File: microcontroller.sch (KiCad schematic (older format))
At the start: 40 parts, among them P1 SWD, P2 DEBUG_UART, P4 CONN_01X08, P5 CONN_01X08, SW1 SW_PUSH, SW2 SW_PUSH, SW3 SW_PUSH, U2 SN74LVC1G08, U3 STM32F072RB, U4 HDC1080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

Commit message: ready?
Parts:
- removed P4, P5: CONN_01X08, Pin_Headers:Pin_Header_Straight_1x08, symbol CONN_01X08
- added P4, P5: CONN_02X05, CAN_Node:PIN_Header_SMD_2.54mm_02x05, symbol CONN_02X05
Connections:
- wire segments 170 -> 176

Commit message: Use micro match for debug connector.
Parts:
- removed P1: SWD, Pin_Headers:Pin_Header_Straight_1x05, symbol CONN_01X05
- removed P2: DEBUG_UART, Pin_Headers:Pin_Header_Straight_1x03, symbol CONN_01X03
- added P1: Debug, CAN_Node:micromatch_smd_2x05, symbol CONN_02X05
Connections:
- wire segments 176 -> 184

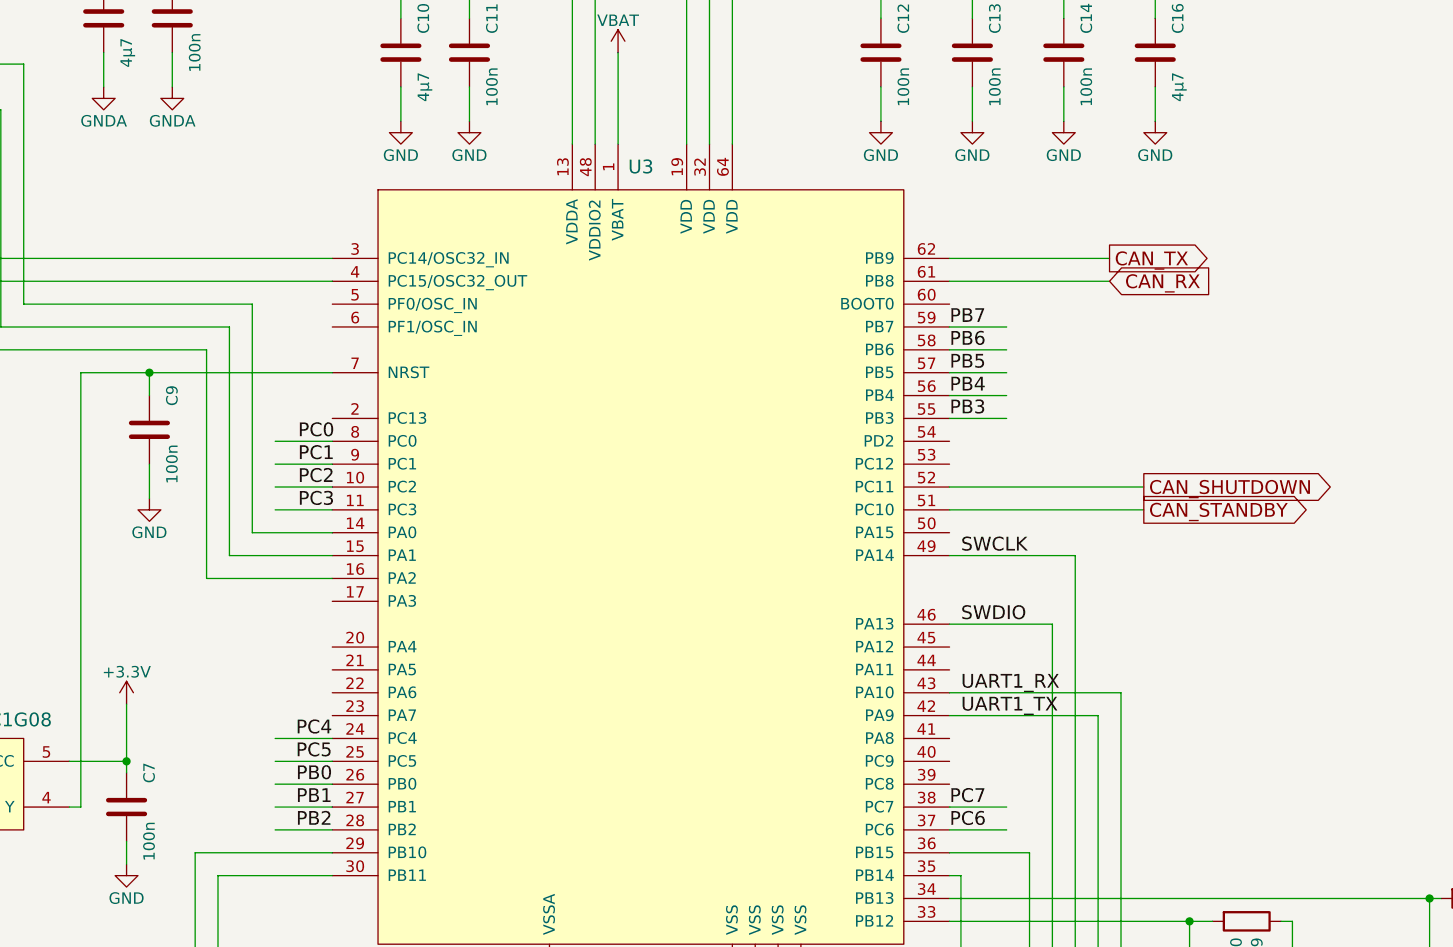
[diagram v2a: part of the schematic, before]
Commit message: Add measurement points, copyright label, minor changes.
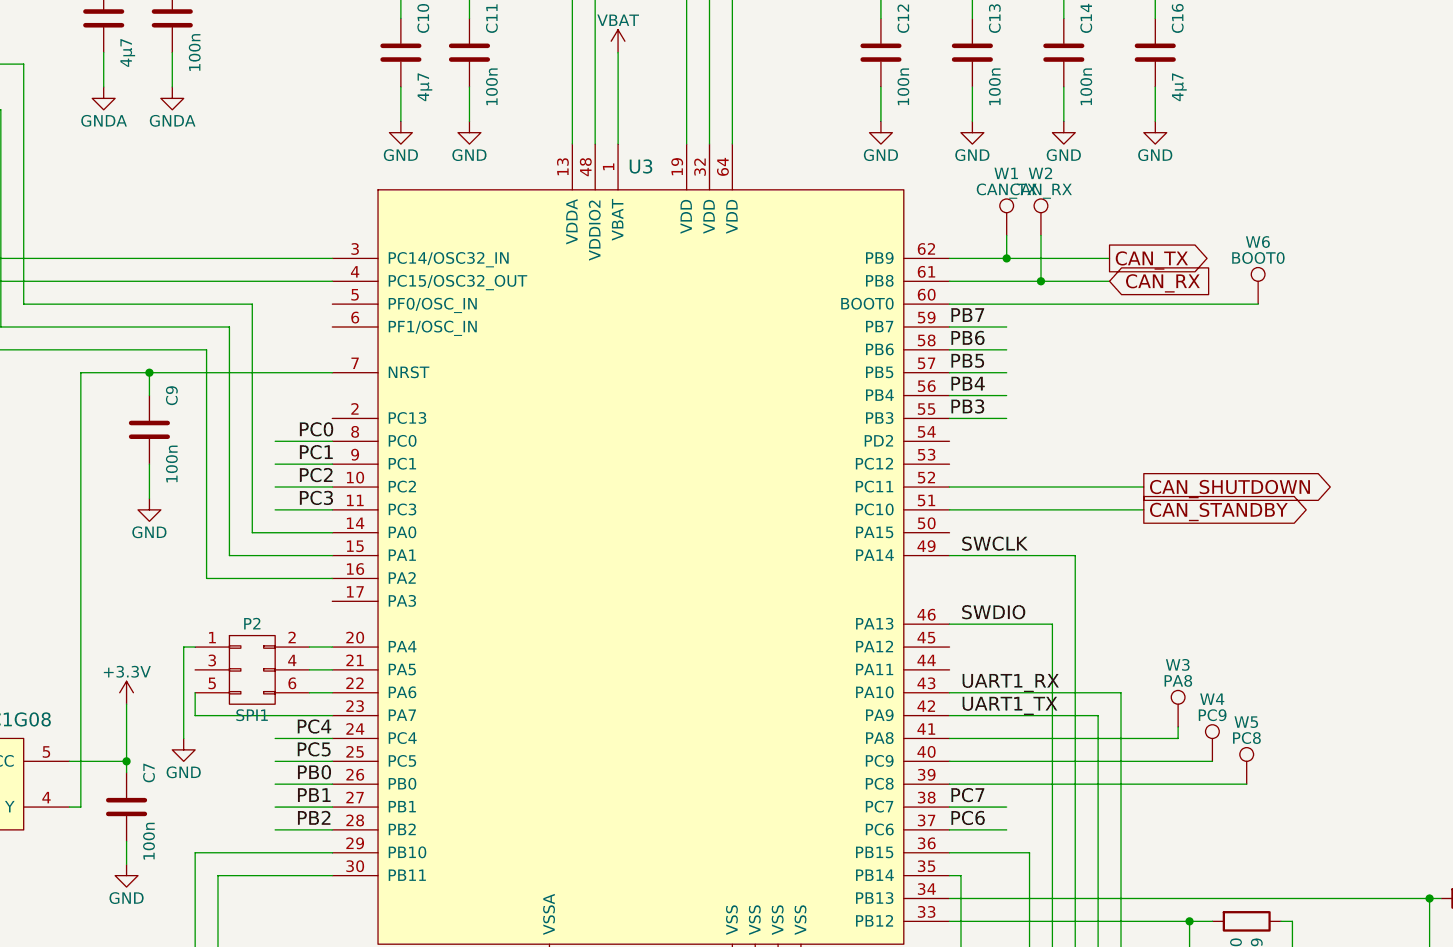
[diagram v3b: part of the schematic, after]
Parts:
- added P2: SPI1, can-node:PIN_Header_SMD_2.54mm_02x03, symbol CONN_02X03
- added W1: CAN_TX, can-node:Measurement_Point_tiny, symbol TEST_1P
- added W2: CAN_RX, can-node:Measurement_Point_tiny, symbol TEST_1P
- added W3: PA8, can-node:Measurement_Point_tiny, symbol TEST_1P
- added W4: PC9, can-node:Measurement_Point_tiny, symbol TEST_1P
- added W5: PC8, can-node:Measurement_Point_tiny, symbol TEST_1P
- added W6: BOOT0, can-node:Measurement_Point_tiny, symbol TEST_1P
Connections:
- wire segments 184 -> 198

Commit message: Add ambient light sensor, minor layout optimizations.
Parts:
- added Q?: SFH3711, SFH3711, symbol OPTO_NPN
- added R?: 4.7k, symbol R
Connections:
- net labels added: ADC_IN3
- wire segments 198 -> 232
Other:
- note added: "ambient light sensor"
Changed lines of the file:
@@
 LIBS:can-node
 LIBS:can-node-cache
-EELAYER 25 0
+EELAYER 26 0
 EELAYER END
 $Descr A4 11693 8268
@@
 	4750 1700 4750 1300
 Wire Wire Line
-	950  2200 950  2900
-Wire Wire Line
-	1800 2300 1800 2900
+	950  2200 950  2550
+Wire Wire Line
+	950  2550 950  2900
+Wire Wire Line
+	1800 2300 1800 2550
+Wire Wire Line
+	1800 2550 1800 2900
 Wire Wire Line
 	1300 2550 950  2550
@@
 	5250 5400 5250 5550
 Wire Wire Line
-	5250 5550 5550 5550
+	5250 5550 5350 5550
+Wire Wire Line
+	5350 5550 5450 5550
+Wire Wire Line
+	5450 5550 5550 5550
 Wire Wire Line
 	5550 5550 5550 5400
 Wire Wire Line
-	5350 5400 5350 5600
+	5350 5400 5350 5550
+Wire Wire Line
+	5350 5550 5350 5600
 Connection ~ 5350 5550
 Wire Wire Line
@@
 Connection ~ 5450 5550
 Wire Wire Line
-	6900 2200 6200 2200
-Wire Wire Line
-	6200 2300 6900 2300
+	6200 2200 6450 2200
+Wire Wire Line
+	6450 2200 6900 2200
+Wire Wire Line
+	6200 2300 6600 2300
+Wire Wire Line
+	6600 2300 6900 2300
 Wire Wire Line
 	2950 3600 3500 3600
@@
 	4700 7300 4700 7400
 Wire Wire Line
-	4700 6450 4700 7000
+	4700 6450 4700 6900
+Wire Wire Line
+	4700 6900 4700 7000
 Wire Wire Line
 	4700 6900 4600 6900
@@
 	2400 4600 2400 2700
 Wire Wire Line
-	2400 2700 3500 2700
+	2400 2700 2700 2700
+Wire Wire Line
+	2700 2700 3500 2700
 Wire Wire Line
 	2350 4400 2600 4400
 Wire Wire Line
-	2600 4150 2600 4450
+	2600 4150 2600 4400
+Wire Wire Line
+	2600 4400 2600 4450
 Wire Wire Line
 	2600 4850 2600 4750
@@
 	8300 6250 8300 5800
 Wire Wire Line
-	7100 750  7100 1150
+	7100 750  7100 950
+Wire Wire Line
+	7100 950  7100 1000
+Wire Wire Line
+	7100 1000 7100 1050
+Wire Wire Line
+	7100 1050 7100 1150
 Wire Wire Line
 	5900 1150 5900 1050
 Wire Wire Line
-	5250 1050 7100 1050
+	5250 1050 5900 1050
+Wire Wire Line
+	5900 1050 7100 1050
 Wire Wire Line
 	5250 1050 5250 1700
@@
 	6300 1150 6300 1000
 Wire Wire Line
-	5150 1000 7100 1000
+	5150 1000 6300 1000
+Wire Wire Line
+	6300 1000 7100 1000
 Wire Wire Line
 	5150 1000 5150 1700
@@
 	5050 1700 5050 950
 Wire Wire Line
-	5050 950  7100 950
+	5050 950  6700 950
+Wire Wire Line
+	6700 950  7100 950
 Wire Wire Line
 	6700 950  6700 1150
@@
 	4650 1050 4650 1700
 Wire Wire Line
-	3800 1050 4650 1050
+	3800 1050 4100 1050
+Wire Wire Line
+	4100 1050 4650 1050
 Wire Wire Line
 	4100 1050 4100 1150
 Wire Wire Line
-	3800 800  3800 1150
+	3800 800  3800 1050
+Wire Wire Line
+	3800 1050 3800 1150
 Connection ~ 4100 1050
 Connection ~ 3800 1050
@@
 	2800 1450 2800 1300
 Wire Wire Line
-	2500 900  4550 900
+	2500 900  2800 900
+Wire Wire Line
+	2800 900  4550 900
 Wire Wire Line
 	2800 900  2800 1000
 Wire Wire Line
-	2500 800  2500 1000
+	2500 800  2500 900
+Wire Wire Line
+	2500 900  2500 1000
 Connection ~ 2800 900
 Connection ~ 2500 900
@@
 	1600 4850 1600 4600
 Wire Wire Line
-	1200 4250 1200 5050
+	1200 4250 1200 4400
+Wire Wire Line
+	1200 4400 1200 5050
 Wire Wire Line
 	1200 4400 1600 4400
 Wire Wire Line
-	1500 4250 1500 7000
+	1500 4250 1500 4500
+Wire Wire Line
+	1500 4500 1500 7000
 Wire Wire Line
 	1500 4500 1600 4500
@@
 	6200 4600 6450 4600
 Wire Wire Line
-	6200 5000 8350 5000
-Wire Wire Line
-	6200 5100 7350 5100
+	6200 5000 8300 5000
+Wire Wire Line
+	8300 5000 8350 5000
+Wire Wire Line
+	6200 5100 7250 5100
+Wire Wire Line
+	7250 5100 7350 5100
 Wire Wire Line
 	6250 4900 6200 4900
@@
 	2900 4800 3500 4800
 Wire Wire Line
-	3000 6800 3600 6800
+	3000 6800 3450 6800
+Wire Wire Line
+	3450 6800 3600 6800
 Wire Wire Line
 	3500 4500 3250 4500
@@
 	2900 4800 2900 6450
 Wire Wire Line
-	2900 6450 4600 6450
+	2900 6450 3800 6450
+Wire Wire Line
+	3800 6450 4600 6450
 Wire Wire Line
 	4600 6450 4600 6800
@@
 	1050 1750 1150 1750
 Wire Wire Line
-	650  1350 650  2000
+	650  1350 650  1550
+Wire Wire Line
+	650  1550 650  1750
+Wire Wire Line
+	650  1750 650  2000
 Wire Wire Line
 	650  1350 750  1350
@@
 Wire Wire Line
 	7550 2400 6200 2400
+$Comp
+L OPTO_NPN Q?
+U 1 1 5862349E
+P 9550 4650
+F 0 "Q?" H 9700 4700 50  0000 L CNN
+F 1 "SFH3711" H 9700 4550 50  0000 L CNN
+F 2 "SFH3711" H 9550 4650 50  0000 C CNN
+F 3 "" H 9550 4650 50  0000 C CNN
+	1    9550 4650
+	1    0    0    -1
+$EndComp
+$Comp
+L R R?
+U 1 1 58623B77
+P 9650 5100
+F 0 "R?" V 9730 5100 50  0000 C CNN
+F 1 "4.7k" V 9650 5100 50  0000 C CNN
+F 2 "" V 9580 5100 50  0000 C CNN
+F 3 "" H 9650 5100 50  0000 C CNN
+	1    9650 5100
+	1    0    0    -1
+$EndComp
+$Comp
+L +3.3V #PWR?
+U 1 1 58623F5A
+P 9650 4300
+F 0 "#PWR?" H 9650 4150 50  0001 C CNN
+F 1 "+3.3V" H 9650 4440 50  0000 C CNN
+F 2 "" H 9650 4300 60  0000 C CNN
+F 3 "" H 9650 4300 60  0000 C CNN
+	1    9650 4300
+	1    0    0    -1
+$EndComp
+Wire Wire Line
+	9650 4300 9650 4450
+$Comp
+L GND #PWR?
+U 1 1 586242DC
+P 9650 5300
+F 0 "#PWR?" H 9650 5050 50  0001 C CNN
+F 1 "GND" H 9650 5150 50  0000 C CNN
+F 2 "" H 9650 5300 60  0000 C CNN
+F 3 "" H 9650 5300 60  0000 C CNN
+	1    9650 5300
+	1    0    0    -1
+$EndComp
+Wire Wire Line
+	9650 4850 9650 4900
+Wire Wire Line
+	9650 4900 9650 4950
+Wire Wire Line
+	9650 5250 9650 5300
+Wire Wire Line
+	3500 3700 3100 3700
+Text Label 3100 3700 0    60   ~ 0
+ADC_IN3
+Wire Wire Line
+	9650 4900 10350 4900
+Connection ~ 9650 4900
+Text Label 10000 4900 0    60   ~ 0
+ADC_IN3
+Wire Notes Line
+	9300 5850 9300 4000
+Wire Notes Line
+	9300 4000 10450 4000
+Wire Notes Line
+	10450 4000 10450 5850
+Wire Notes Line
+	10450 5850 9300 5850
+Text Notes 9400 5800 0    60   ~ 0
+ambient light sensor
 $EndSCHEMATC

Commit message: Add missing schematic changes.
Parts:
- Q2: renamed from Q?; footprint SFH3711 -> can-node:SFH3711; symbol OPTO_NPN -> Q_Photo_NPN_CE
- R18: renamed from R?; footprint (none) -> Resistors_SMD:R_0402
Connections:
- wire segments 232 -> 203
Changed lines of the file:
@@
 	4750 1700 4750 1300
 Wire Wire Line
-	950  2200 950  2550
-Wire Wire Line
-	950  2550 950  2900
-Wire Wire Line
-	1800 2300 1800 2550
-Wire Wire Line
-	1800 2550 1800 2900
+	950  2200 950  2900
+Wire Wire Line
+	1800 2300 1800 2900
 Wire Wire Line
 	1300 2550 950  2550
@@
 	5250 5400 5250 5550
 Wire Wire Line
-	5250 5550 5350 5550
-Wire Wire Line
-	5350 5550 5450 5550
-Wire Wire Line
-	5450 5550 5550 5550
+	5250 5550 5550 5550
 Wire Wire Line
 	5550 5550 5550 5400
 Wire Wire Line
-	5350 5400 5350 5550
-Wire Wire Line
-	5350 5550 5350 5600
+	5350 5400 5350 5600
 Connection ~ 5350 5550
 Wire Wire Line
@@
 Connection ~ 5450 5550
 Wire Wire Line
-	6200 2200 6450 2200
-Wire Wire Line
-	6450 2200 6900 2200
-Wire Wire Line
-	6200 2300 6600 2300
-Wire Wire Line
-	6600 2300 6900 2300
+	6200 2200 6900 2200
+Wire Wire Line
+	6200 2300 6900 2300
 Wire Wire Line
 	2950 3600 3500 3600
@@
 	4700 7300 4700 7400
 Wire Wire Line
-	4700 6450 4700 6900
-Wire Wire Line
-	4700 6900 4700 7000
+	4700 6450 4700 7000
 Wire Wire Line
 	4700 6900 4600 6900
@@
 	2400 4600 2400 2700
 Wire Wire Line
-	2400 2700 2700 2700
-Wire Wire Line
-	2700 2700 3500 2700
+	2400 2700 3500 2700
 Wire Wire Line
 	2350 4400 2600 4400
 Wire Wire Line
-	2600 4150 2600 4400
-Wire Wire Line
-	2600 4400 2600 4450
+	2600 4150 2600 4450
 Wire Wire Line
 	2600 4850 2600 4750
@@
 	8300 6250 8300 5800
 Wire Wire Line
-	7100 750  7100 950
-Wire Wire Line
-	7100 950  7100 1000
-Wire Wire Line
-	7100 1000 7100 1050
-Wire Wire Line
-	7100 1050 7100 1150
+	7100 750  7100 1150
 Wire Wire Line
 	5900 1150 5900 1050
 Wire Wire Line
-	5250 1050 5900 1050
-Wire Wire Line
-	5900 1050 7100 1050
+	5250 1050 7100 1050
 Wire Wire Line
 	5250 1050 5250 1700
@@
 	6300 1150 6300 1000
 Wire Wire Line
-	5150 1000 6300 1000
-Wire Wire Line
-	6300 1000 7100 1000
+	5150 1000 7100 1000
 Wire Wire Line
 	5150 1000 5150 1700
@@
 	5050 1700 5050 950
 Wire Wire Line
-	5050 950  6700 950
-Wire Wire Line
-	6700 950  7100 950
+	5050 950  7100 950
 Wire Wire Line
 	6700 950  6700 1150
@@
 	4650 1050 4650 1700
 Wire Wire Line
-	3800 1050 4100 1050
-Wire Wire Line
-	4100 1050 4650 1050
+	3800 1050 4650 1050
 Wire Wire Line
 	4100 1050 4100 1150
 Wire Wire Line
-	3800 800  3800 1050
-Wire Wire Line
-	3800 1050 3800 1150
+	3800 800  3800 1150
 Connection ~ 4100 1050
 Connection ~ 3800 1050
@@
 	2800 1450 2800 1300
 Wire Wire Line
-	2500 900  2800 900
-Wire Wire Line
-	2800 900  4550 900
+	2500 900  4550 900
 Wire Wire Line
 	2800 900  2800 1000
 Wire Wire Line
-	2500 800  2500 900
-Wire Wire Line
-	2500 900  2500 1000
+	2500 800  2500 1000
 Connection ~ 2800 900
 Connection ~ 2500 900
@@
 	1600 4850 1600 4600
 Wire Wire Line
-	1200 4250 1200 4400
-Wire Wire Line
-	1200 4400 1200 5050
+	1200 4250 1200 5050
 Wire Wire Line
 	1200 4400 1600 4400
 Wire Wire Line
-	1500 4250 1500 4500
-Wire Wire Line
-	1500 4500 1500 7000
+	1500 4250 1500 7000
 Wire Wire Line
 	1500 4500 1600 4500
@@
 	6200 4600 6450 4600
 Wire Wire Line
-	6200 5000 8300 5000
-Wire Wire Line
-	8300 5000 8350 5000
-Wire Wire Line
-	6200 5100 7250 5100
-Wire Wire Line
-	7250 5100 7350 5100
+	6200 5000 8350 5000
+Wire Wire Line
+	6200 5100 7350 5100
 Wire Wire Line
 	6250 4900 6200 4900
@@
 	2900 4800 3500 4800
 Wire Wire Line
-	3000 6800 3450 6800
-Wire Wire Line
-	3450 6800 3600 6800
+	3000 6800 3600 6800
 Wire Wire Line
 	3500 4500 3250 4500
@@
 	2900 4800 2900 6450
 Wire Wire Line
-	2900 6450 3800 6450
-Wire Wire Line
-	3800 6450 4600 6450
+	2900 6450 4600 6450
 Wire Wire Line
 	4600 6450 4600 6800
@@
 	1050 1750 1150 1750
 Wire Wire Line
-	650  1350 650  1550
-Wire Wire Line
-	650  1550 650  1750
-Wire Wire Line
-	650  1750 650  2000
+	650  1350 650  2000
 Wire Wire Line
 	650  1350 750  1350
@@
 	7550 2400 6200 2400
 $Comp
-L OPTO_NPN Q?
+L Q_Photo_NPN_CE Q2
 U 1 1 5862349E
 P 9550 4650
-F 0 "Q?" H 9700 4700 50  0000 L CNN
+F 0 "Q2" H 9700 4700 50  0000 L CNN
 F 1 "SFH3711" H 9700 4550 50  0000 L CNN
-F 2 "SFH3711" H 9550 4650 50  0000 C CNN
+F 2 "can-node:SFH3711" H 9550 4650 50  0000 C CNN
 F 3 "" H 9550 4650 50  0000 C CNN
 	1    9550 4650
@@
 $EndComp
 $Comp
-L R R?
+L R R18
 U 1 1 58623B77
 P 9650 5100
-F 0 "R?" V 9730 5100 50  0000 C CNN
+F 0 "R18" V 9730 5100 50  0000 C CNN
 F 1 "4.7k" V 9650 5100 50  0000 C CNN
-F 2 "" V 9580 5100 50  0000 C CNN
+F 2 "Resistors_SMD:R_0402" V 9580 5100 50  0001 C CNN
 F 3 "" H 9650 5100 50  0000 C CNN
 	1    9650 5100
@@
 $EndComp
 $Comp
-L +3.3V #PWR?
+L +3.3V #PWR058
 U 1 1 58623F5A
 P 9650 4300
-F 0 "#PWR?" H 9650 4150 50  0001 C CNN
+F 0 "#PWR058" H 9650 4150 50  0001 C CNN
 F 1 "+3.3V" H 9650 4440 50  0000 C CNN
 F 2 "" H 9650 4300 60  0000 C CNN
@@
 	9650 4300 9650 4450
 $Comp
-L GND #PWR?
+L GND #PWR059
 U 1 1 586242DC
 P 9650 5300
-F 0 "#PWR?" H 9650 5050 50  0001 C CNN
+F 0 "#PWR059" H 9650 5050 50  0001 C CNN
 F 1 "GND" H 9650 5150 50  0000 C CNN
 F 2 "" H 9650 5300 60  0000 C CNN
@@
 $EndComp
 Wire Wire Line
-	9650 4850 9650 4900
-Wire Wire Line
-	9650 4900 9650 4950
+	9650 4850 9650 4950
 Wire Wire Line
 	9650 5250 9650 5300
